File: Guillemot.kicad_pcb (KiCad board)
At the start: 4 copper layers, 52.3 x 27.8 mm, 32 parts, among them Q1 IPB042N10N3G, Q2 AO3422, Q3 SI2309CDS, Q4 2N7002, Q5 MMBT3904, Q6 MMBT3904, U1 XIAO-nRF52840-SMD, U2 SN74LVC2G02DCTR

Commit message: Add PROTOCOL.md, Whimbrel provisioning, build fix (TinyUSB/SPI/bonding), config placeholders
Made-with: Cursor
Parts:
- added TP6: 3.3V, TestPoint:TestPoint_Pad_2.0x2.0mm, F.Cu at (120.0, 60.8)
- added TP7: GND, TestPoint:TestPoint_Pad_2.0x2.0mm, F.Cu at (123.0, 60.8)
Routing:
- net /3.3V: track 60.7 -> 74.4 mm, vias 4 -> 5
- net GND: vias 52 -> 53

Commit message: Update KiCad PCB
Made-with: Cursor
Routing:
- net /ESC-: vias 53 -> 49
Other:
- outline, holes or cut-outs redrawn
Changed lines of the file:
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@@
 		)
+	)
+	(gr_circle
+		(center 93 61)
+		(end 94 61)
+		(stroke
+			(width 0.05)
+			(type solid)
+		)
+		(fill no)
+		(layer "Edge.Cuts")
+	)
+	(gr_circle
+		(center 141 61)
+		(end 142 61)
+		(stroke
+			(width 0.05)
+			(type solid)
+		)
+		(fill no)
+		(layer "Edge.Cuts")
 	)
 	(gr_rect
@@
 		(layer "Edge.Cuts")
 	)
+	(gr_circle
+		(center 93 37)
+		(end 94 37)
+		(stroke
+			(width 0.05)
+			(type solid)
+		)
+		(fill no)
+		(layer "Edge.Cuts")
+	)
 	(segment
 		(start 122.68 54.25)
@@
 	)
 	(via
-		(at 92.5 59.25)
-		(size 0.6)
-		(drill 0.3)
-		(layers "F.Cu" "B.Cu")
-		(free yes)
-		(net 11)
-	)
-	(via
 		(at 101.5 44.5)
 		(size 0.6)
@@
 	)
 	(via
-		(at 94 60.75)
-		(size 0.6)
-		(drill 0.3)
-		(layers "F.Cu" "B.Cu")
-		(free yes)
-		(net 11)
-	)
-	(via
 		(at 103 46)
 		(size 0.6)
@@
 	)
 	(via
-		(at 92.5 60.75)
-		(size 0.6)
-		(drill 0.3)
-		(layers "F.Cu" "B.Cu")
-		(free yes)
-		(net 11)
-	)
-	(via
 		(at 95 54.75)
 		(size 0.6)
@@
 		(size 0.6)
 		(drill 0.3)
-		(layers "F.Cu" "B.Cu")
-		(free yes)
-		(net 11)
-	)
-	(via
-		(at 94 59.25)
-		(size 0.6)
-		(drill 0.3)

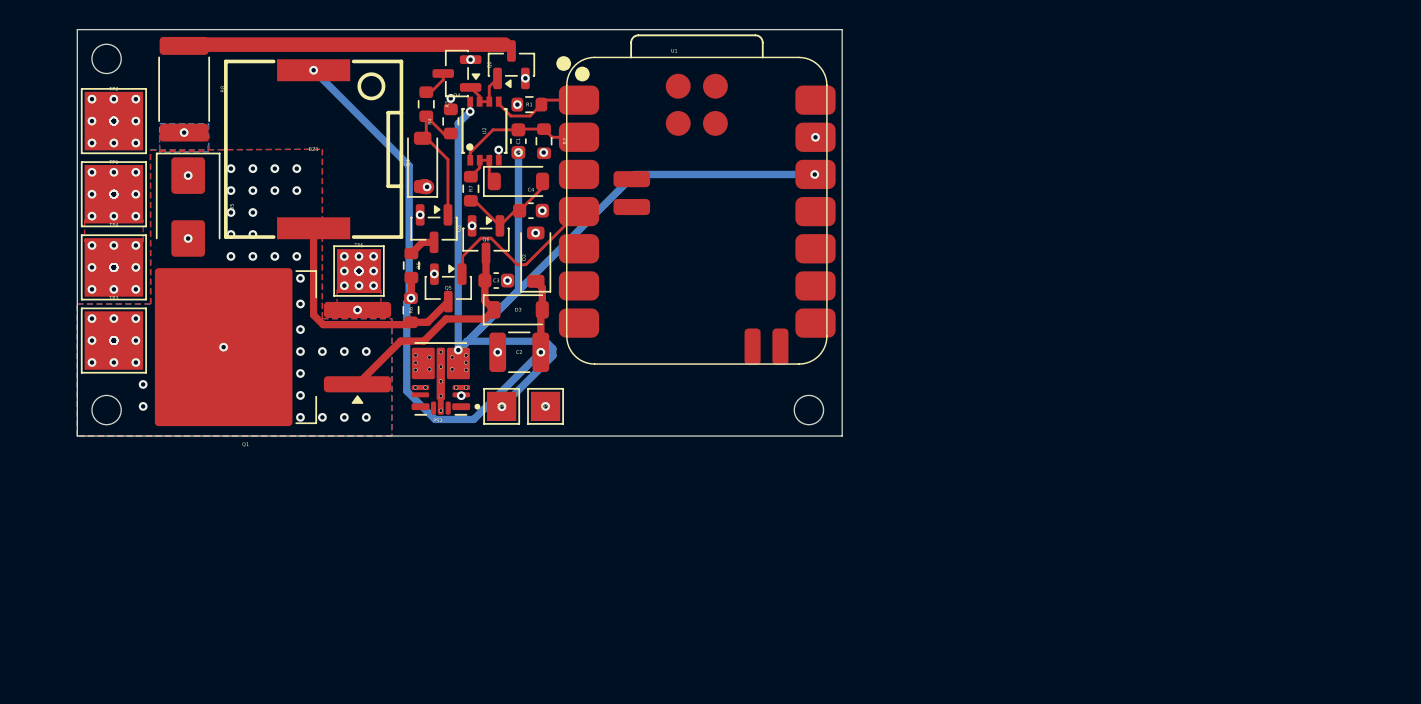
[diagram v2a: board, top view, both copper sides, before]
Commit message: Update KiCad project, README, production outputs; add fix_readme_cost.py
Made-with: Cursor
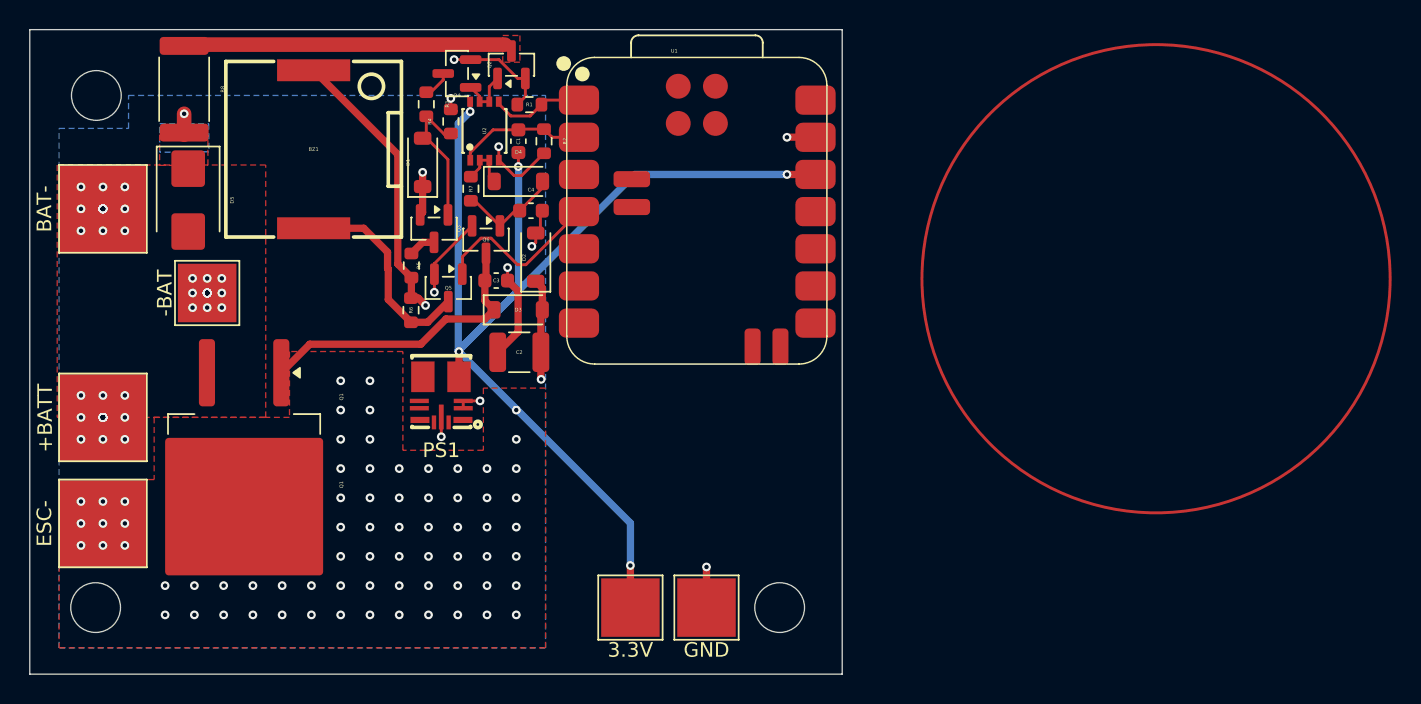
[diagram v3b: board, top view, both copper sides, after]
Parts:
- removed TP1: BAT+, TestPoint:TestPoint_Pad_4.0x4.0mm
- +BATT: renamed from TP4; footprint TestPoint:TestPoint_Pad_4.0x4.0mm -> TestPoint:TestPoint_Pad_6.0x6.0mm
- -BAT: renamed from TP5; footprint TestPoint:TestPoint_Pad_3.0x3.0mm -> TestPoint:TestPoint_Pad_4.0x4.0mm
- 3.3V: renamed from TP6; footprint TestPoint:TestPoint_Pad_2.0x2.0mm -> TestPoint:TestPoint_Pad_4.0x4.0mm
- BAT-: renamed from TP2; footprint TestPoint:TestPoint_Pad_4.0x4.0mm -> TestPoint:TestPoint_Pad_6.0x6.0mm
- ESC-: renamed from TP3; footprint TestPoint:TestPoint_Pad_4.0x4.0mm -> TestPoint:TestPoint_Pad_6.0x6.0mm
- GND: renamed from TP7; footprint TestPoint:TestPoint_Pad_2.0x2.0mm -> TestPoint:TestPoint_Pad_4.0x4.0mm
- PS1: footprint TPSM365R6V3RDNR:CONV_TPSM365R6V3RDNR -> easyeda2kicad:QFN-11_L4.5-W3.5-P0.50-TL_TPSM365R6FRDNR
- moved GND 17.6 mm to (134.0, 74.5), turned to 180 degrees
- moved 3.3V 16.3 mm to (128.8, 74.5), turned to 180 degrees
- moved ESC- 12.5 mm to (92.8, 68.8), turned to 90 degrees
- moved -BAT 10.5 mm to (99.9, 53.0), turned to 90 degrees
- moved +BATT 10.3 mm to (92.8, 61.5), turned to 90 degrees
- moved Q1 9.40 mm to (102.4, 66.1), turned to -90 degrees
- moved BAT- 6.05 mm to (92.8, 47.2), turned to 90 degrees
- moved PS1 1.48 mm to (115.9, 60.3)
- moved D5 0.48 mm to (98.6, 46.6)
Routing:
- net GND: track 18.4 -> 49.2 mm, vias 53 -> 45
- net /3.3V: track 74.4 -> 86.3 mm, vias 5 -> 6
- net /10V_RAIL: track 43.2 -> 36.5 mm, vias 3 -> 2
- net /ISO_GATE: track 15.6 -> 20.5 mm
- net +BATT: track 1.55 -> 5.81 mm, vias 38 -> 20
- net /BUZZER_SINK: track 16.7 -> 15.0 mm
- net /ESC-: track 0.71 -> 1.90 mm, vias 49 -> 71
- added copper zone on F.Cu, net /PRECHARGE_OUT
- removed copper zone on F.Cu, net +BATT
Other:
- board size 52.3 x 27.8 mm -> 55.5 x 44 mm
- board text added: "Q1"

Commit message: docs: add architecture critique, update readme and pcb files
Made-with: Cursor
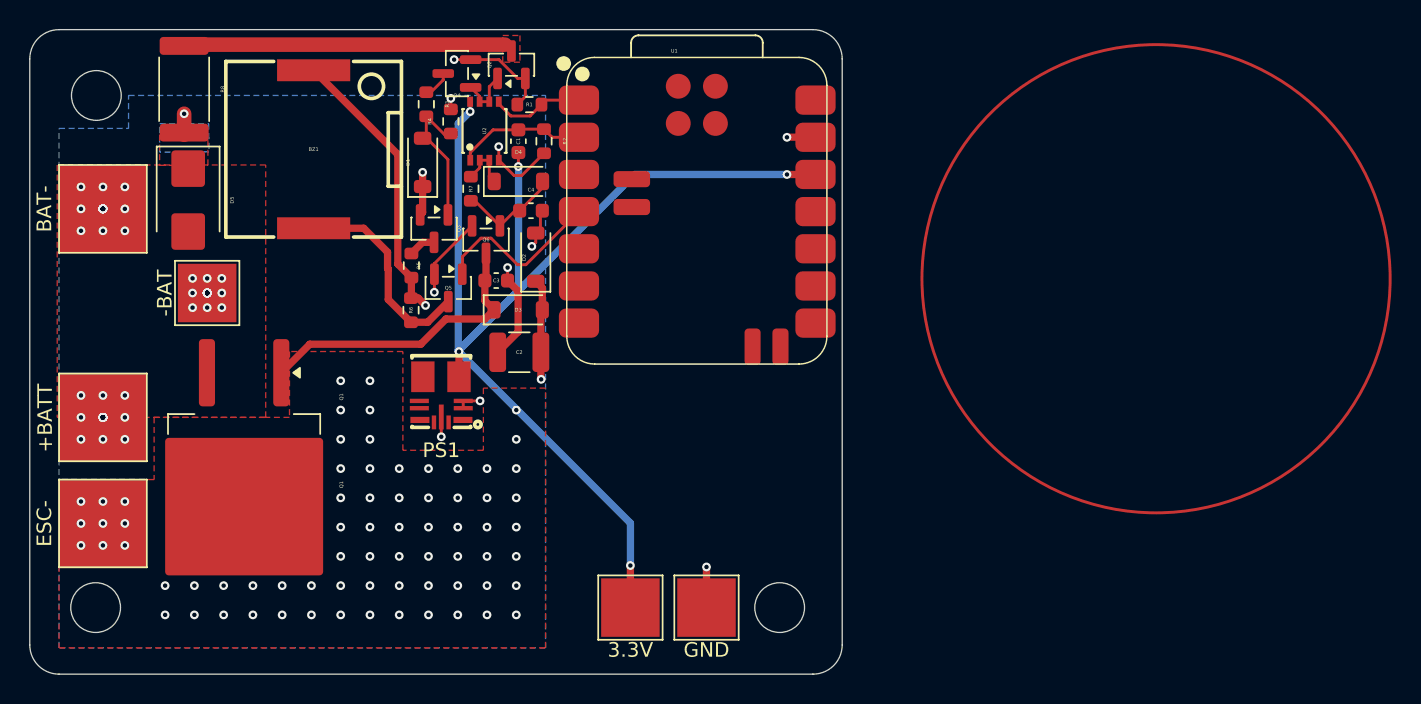
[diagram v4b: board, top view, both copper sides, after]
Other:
- outline, holes or cut-outs redrawn
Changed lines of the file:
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@@
 		(layer "F.Cu")
+	)
+	(gr_arc
+		(start 89.75 79.05)
+		(mid 88.335786 78.464214)
+		(end 87.75 77.05)
+		(stroke
+			(width 0.05)
+			(type default)
+		)
+		(layer "Edge.Cuts")
 	)
 	(gr_circle
@@
 		(layer "Edge.Cuts")
 	)
-	(gr_rect
-		(start 87.75 35)
-		(end 143.275 79.05)
+	(gr_arc
+		(start 87.75 37)
+		(mid 88.335786 35.585786)
+		(end 89.75 35)
 		(stroke
 			(width 0.05)
-			(type solid)
+			(type default)
 		)
-		(fill no)
 		(layer "Edge.Cuts")
 	)
+	(gr_line
+		(start 143.275 37)
+		(end 143.275 77.05)
+		(stroke
+			(width 0.05)
+			(type default)
+		)
+		(layer "Edge.Cuts")
+	)
+	(gr_line
+		(start 141.275 79.05)
+		(end 89.75 79.05)
+		(stroke
+			(width 0.05)
+			(type default)
+		)
+		(layer "Edge.Cuts")
+	)
+	(gr_line
+		(start 89.75 35)
+		(end 141.275 35)
+		(stroke
+			(width 0.05)
+			(type default)
+		)
+		(layer "Edge.Cuts")
+	)
+	(gr_line
+		(start 87.75 77.05)
+		(end 87.75 37)
+		(stroke
+			(width 0.05)
+			(type default)
+		)
+		(layer "Edge.Cuts")
+	)
+	(gr_arc
+		(start 141.275 35)
+		(mid 142.689214 35.585786)
+		(end 143.275 37)
+		(stroke
+			(width 0.05)
+			(type default)
+		)
+		(layer "Edge.Cuts")
+	)
+	(gr_arc
+		(start 143.275 77.05)
+		(mid 142.689214 78.464214)
+		(end 141.275 79.05)
+		(stroke
+			(width 0.05)
+			(type default)
+		)
+		(layer "Edge.Cuts")
+	)
